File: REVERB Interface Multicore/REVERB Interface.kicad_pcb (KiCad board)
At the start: 2 copper layers, 90.2 x 95.9 mm, 71 parts, among them J1 RPiZeroW, J2 Iridium, J3 APRS, J4 Antenna, J5 UPDI, M1 MountingHole_Pad, M2 MountingHole_Pad, M3 MountingHole_Pad, M4 MountingHole_Pad, M5 PiMount, M6 PiMount, M7 PiMount, M8 PiMount, U1 IMU, U2 MAX3232, U3 ATtiny1604-SS, U4 TXB0104D, U5 DS3231BOB, U6 LM1117-3.3

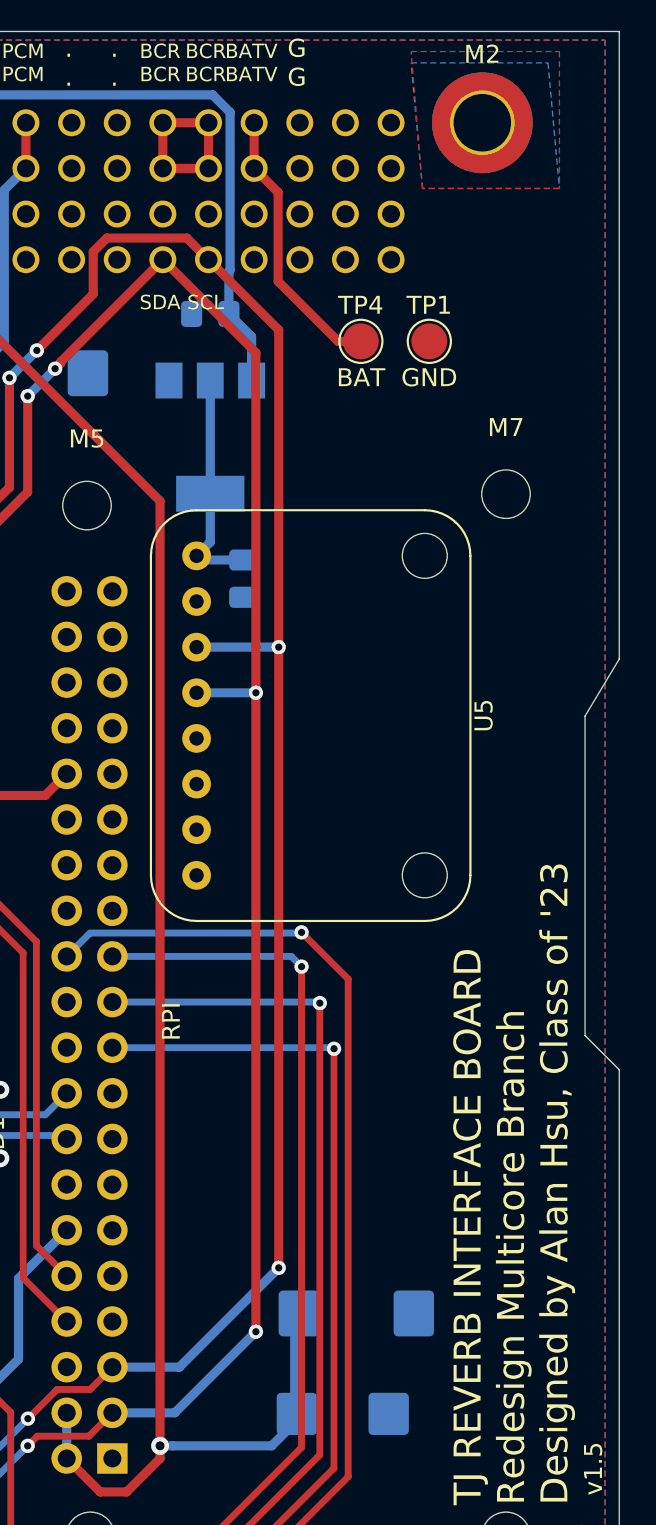
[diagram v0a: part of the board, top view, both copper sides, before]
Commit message: add footprints, may need to use smaller battery
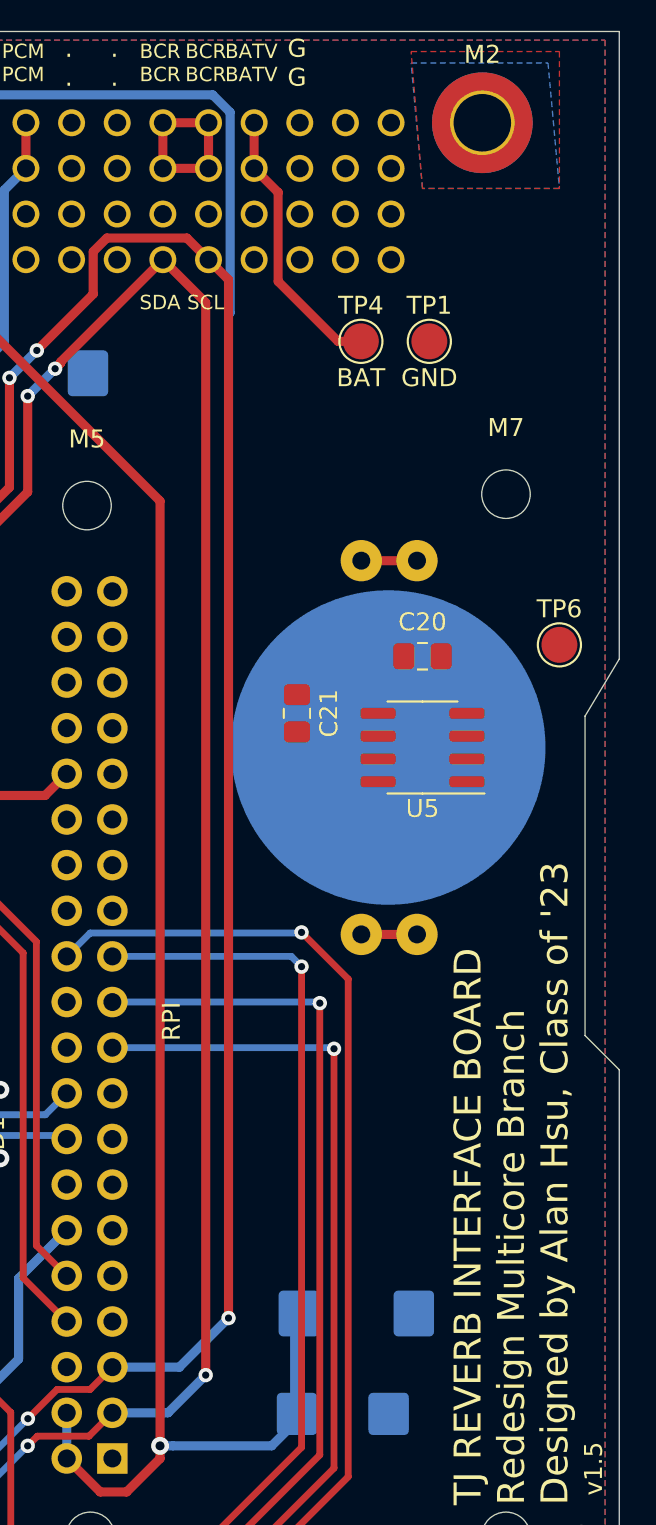
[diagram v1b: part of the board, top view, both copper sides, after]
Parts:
- removed U6: LM1117-3.3, Package_TO_SOT_SMD:SOT-223-3_TabPin2
- added BT1: CR-2032, REVERB Interface:CR2032-LINX-HLD-001-THM, B.Cu at (184.2, 92.7)
- added TP6: SQWV, TestPoint:TestPoint_Pad_D2.0mm, F.Cu at (193.7, 87.0)
- C20, C21: value 10uF -> 1uF; moved to F.Cu
- U5: value DS3231BOB -> DS3232M; footprint REVERB Interface:DS3231BOB -> Package_SO:SOIC-8_3.9x4.9mm_P1.27mm
- moved C20 22.4 mm to (186.1, 87.6)
- moved U5 12.7 mm to (186.1, 92.7), turned to 180 degrees
- moved C21 8.09 mm to (179.1, 90.8), turned to 90 degrees
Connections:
- C20 pad 1: /SW7 -> +3V3
- C21 pad 1: Net-(C21-Pad1) -> Net-(BT1-Pad1)
- H2 pad 16: /SW7 -> (no net)
- U5 pad 1: Net-(C21-Pad1) -> (no net)
- U5 pad 2: GND -> +3V3
- U5 pad 3: /EPSSCL -> /SQW
- U5 pad 4: /EPSSDA -> (no net)
- U5 pad 5: (no net) -> GND
- U5 pad 6: (no net) -> Net-(BT1-Pad1)
- U5 pad 7: (no net) -> /EPSSDA
- U5 pad 8: (no net) -> /EPSSCL
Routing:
- net /SW7: track 53.3 -> 0.00 mm
- net (no net): track 0.00 -> 49.1 mm
- net Net-(C21-Pad1): track 12.7 -> 0.00 mm
- net /EPSSCL: track 175.6 -> 168.7 mm, vias 9 -> 8
- net Net-(BT1-Pad1): track 0.00 -> 6.20 mm
- net /EPSSDA: track 181.2 -> 175.4 mm, vias 8 -> 7

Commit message: 3d model updates
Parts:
- moved C11 2.54 mm to (179.8, 124.2)
- moved C13 2.54 mm to (179.1, 129.8)
- moved C20 0.64 mm to (185.4, 87.6)
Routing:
- net +3V3: track 96.7 -> 156.8 mm
- net (no net): track 49.1 -> 0.00 mm
- net Net-(BT1-Pad1): track 6.20 -> 34.7 mm
- net /EPSSDA: track 175.4 -> 189.8 mm, vias 7 -> 9
- net /EPSSCL: track 168.7 -> 176.7 mm
- net /SQW: track 0.00 -> 7.78 mm
- net /SPISCK: track 72.9 -> 68.0 mm
- net /SPIMISO: track 73.1 -> 68.4 mm
- net /SPIMOSI: track 72.7 -> 68.6 mm
- net /SPICE0: track 87.1 -> 83.5 mm
- net +5V: track 183.5 -> 180.8 mm
- net GND: vias 25 -> 27

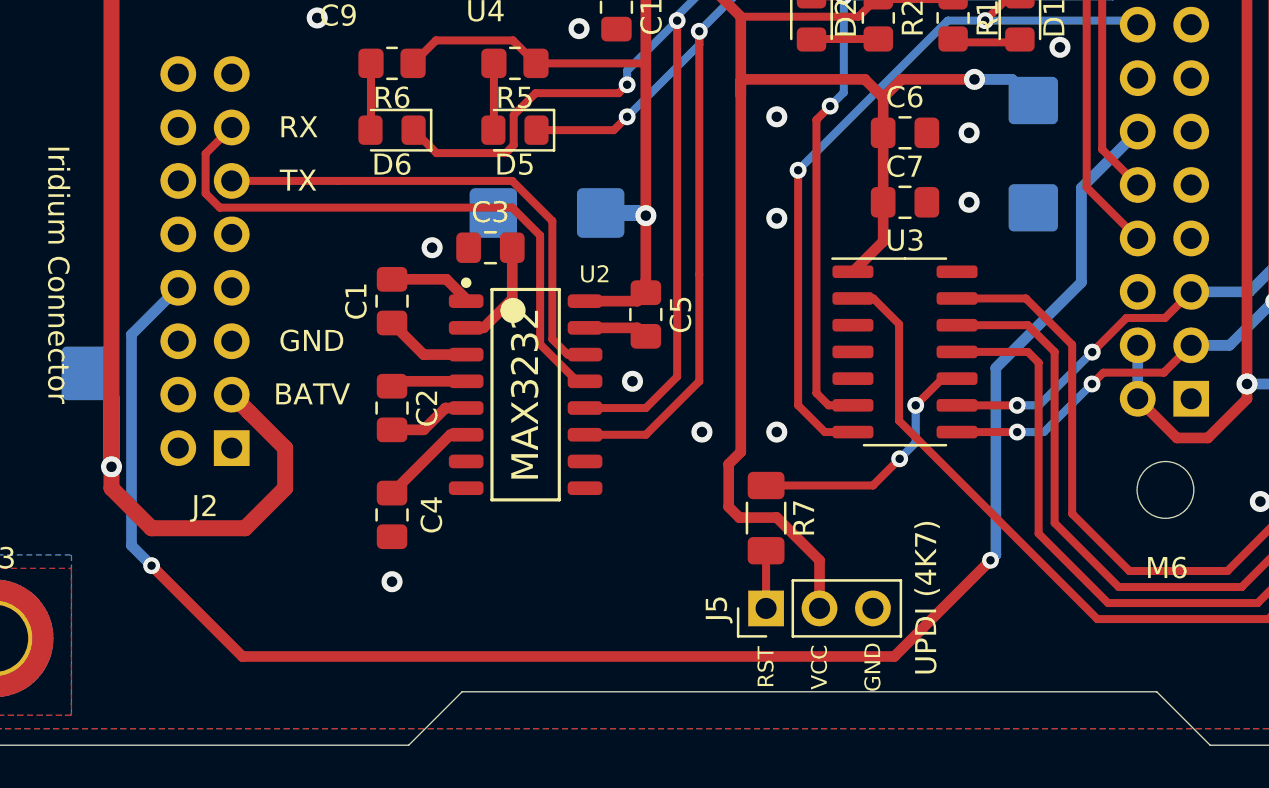
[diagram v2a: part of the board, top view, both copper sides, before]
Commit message: Remove RI line
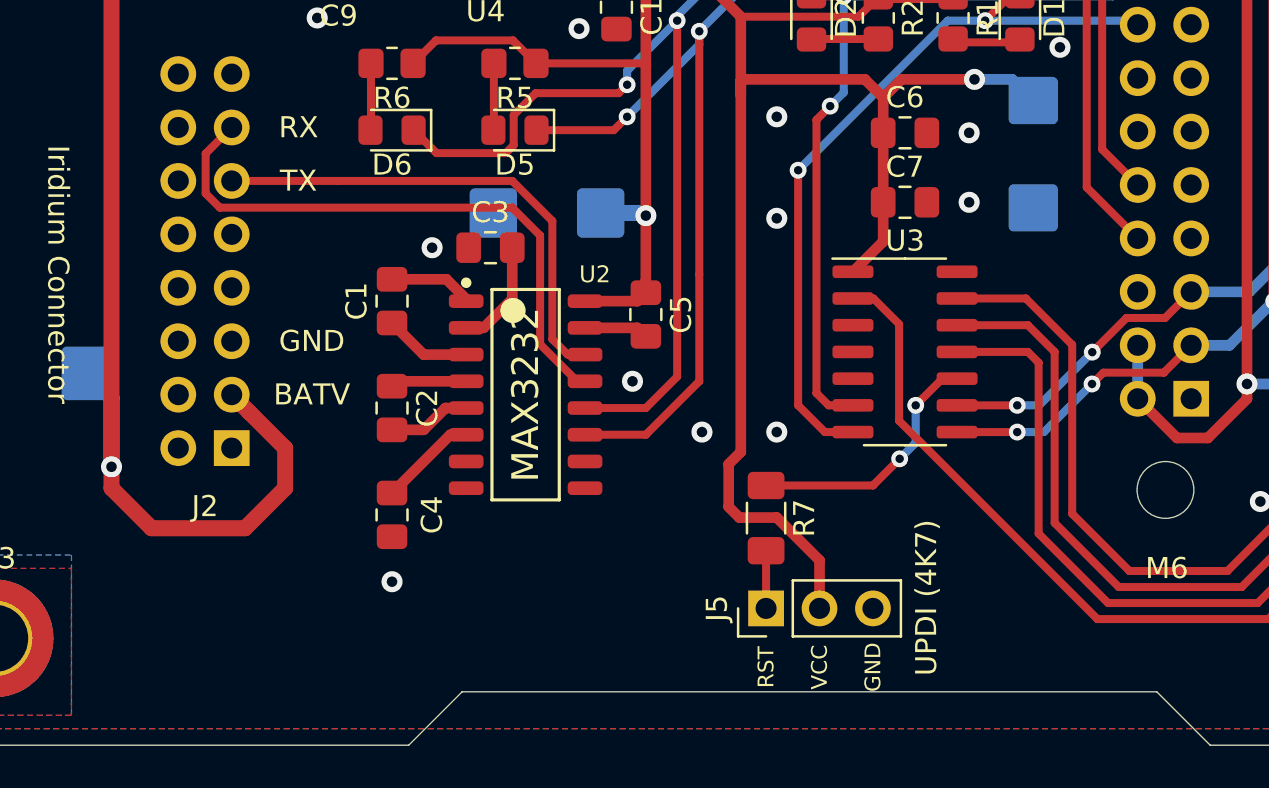
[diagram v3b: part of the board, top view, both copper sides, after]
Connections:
- J1 pad 12: /RI -> (no net)
- J2 pad 8: /RI -> (no net)
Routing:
- net /RI: track 81.4 -> 0.00 mm, vias 2 -> 0

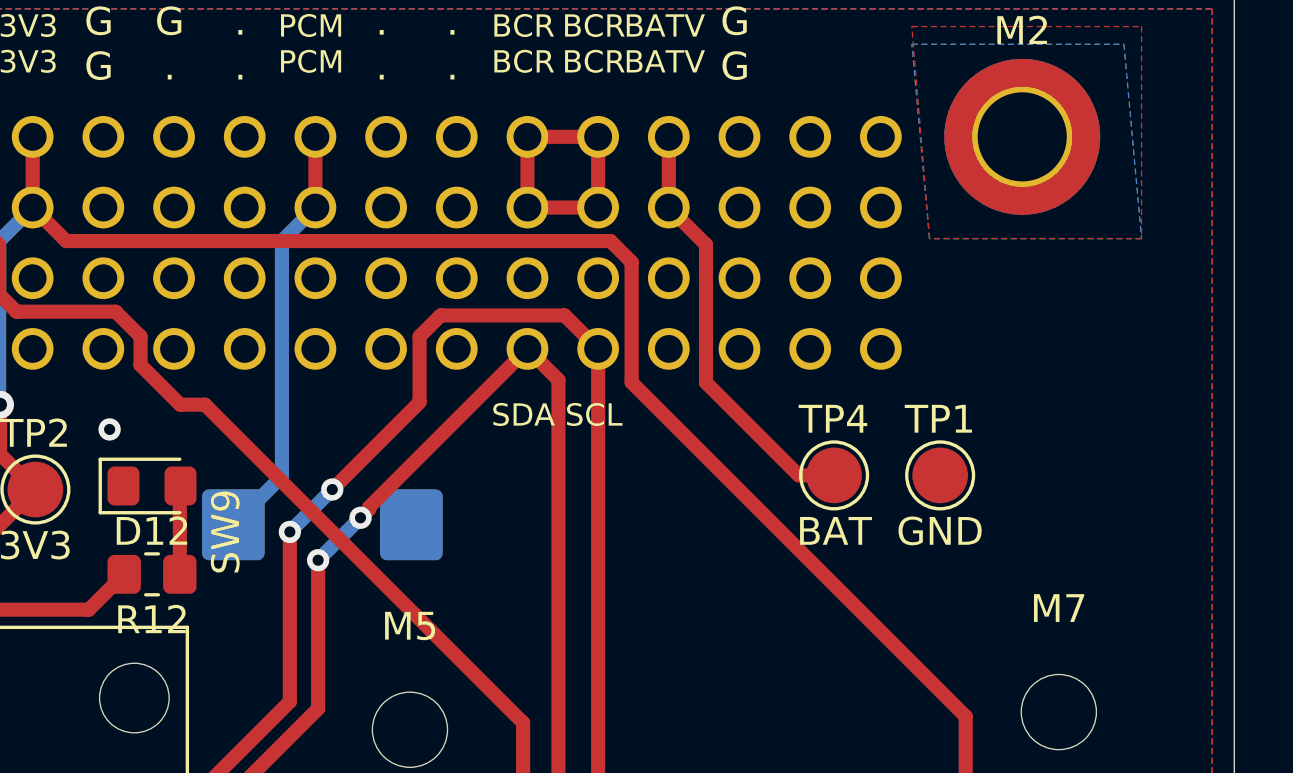
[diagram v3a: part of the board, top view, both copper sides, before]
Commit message: add usb switch
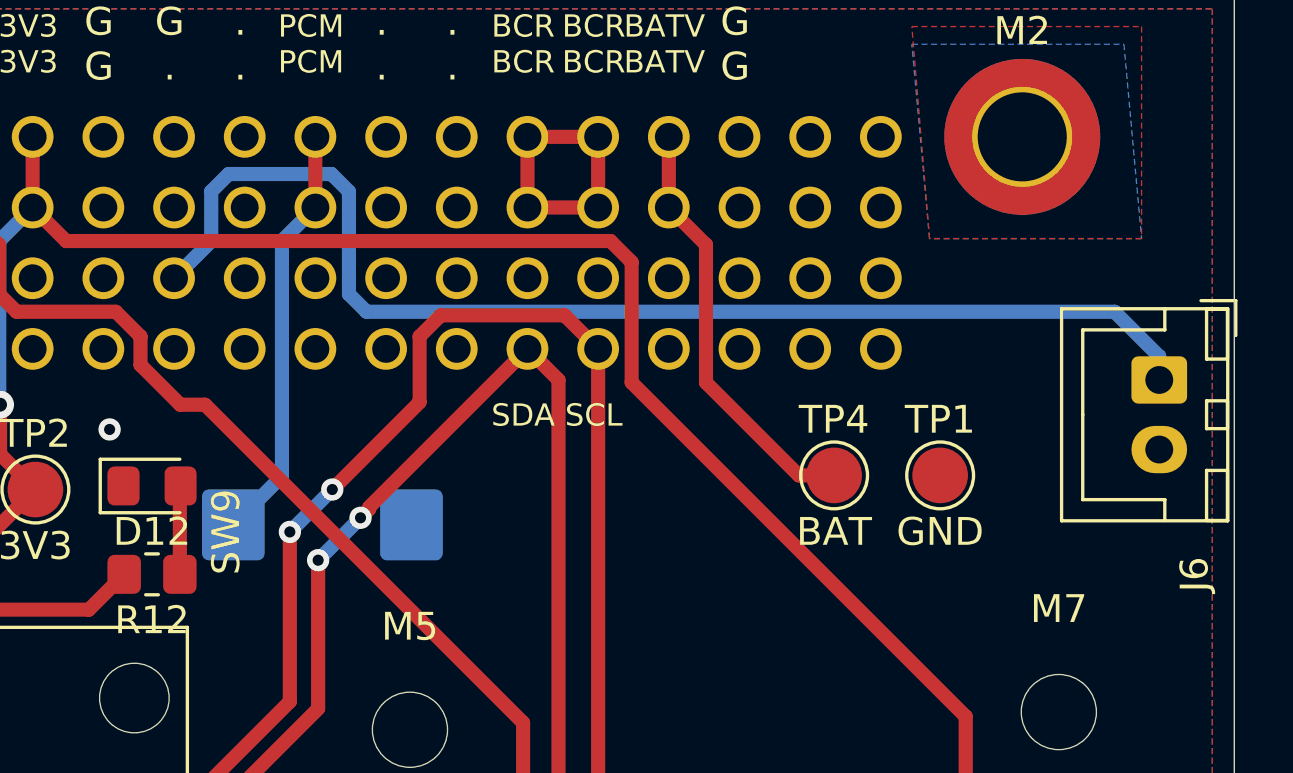
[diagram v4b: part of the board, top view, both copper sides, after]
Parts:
- added J6: USBPWR, Connector_JST:JST_XH_B2B-XH-A_1x02_P2.50mm_Vertical, F.Cu at (194.3, 66.7)
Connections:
- H1 pad 32: (no net) -> /5VUSBCHG
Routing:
- net /5VUSBCHG: track 0.00 -> 43.7 mm

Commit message: Move some parts around, remove UART LEDs, .step export, push v1.6
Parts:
- removed D1, D5: RED, LED_SMD:LED_0805_2012Metric_Pad1.15x1.40mm_HandSolder
- removed D2, D6: GREEN, LED_SMD:LED_0805_2012Metric_Pad1.15x1.40mm_HandSolder
- removed R1, R2, R5, R6: 1K, Resistor_SMD:R_0805_2012Metric_Pad1.20x1.40mm_HandSolder
- moved R11 9.58 mm to (109.2, 70.9), turned to 180 degrees
- moved D11 8.18 mm to (109.2, 74.5), turned to 180 degrees
- moved C9 7.73 mm to (132.1, 119.1), turned to 0 degrees
- moved C10 3.98 mm to (139.7, 117.2)
- moved U4 3.98 mm to (133.5, 112.1)
- moved JP1 3.86 mm to (145.4, 101.6)
- moved JP2 3.86 mm to (154.3, 101.7)
- moved JP3 3.86 mm to (145.4, 108.0)
- moved JP4 3.86 mm to (154.3, 108.0)
- moved C16 3.81 mm to (112.0, 82.3), turned to 270 degrees
- moved C15 3.21 mm to (113.0, 103.5), turned to 90 degrees
- moved J3 3.18 mm to (117.5, 85.1)
- moved J2 3.17 mm to (120.0, 134.6)
- moved BT1 2.29 mm to (181.9, 92.7)
- moved C11 2.29 mm to (177.5, 124.2)
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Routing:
- net /R1OUT: track 52.4 -> 34.6 mm, vias 3 -> 2
- net /T1IN: track 54.2 -> 41.3 mm, vias 3 -> 2
- net /SW10: track 139.2 -> 129.3 mm
- net /SW8: track 100.5 -> 90.8 mm
- net /APRSTXSh: track 24.2 -> 31.0 mm
- net /APRSRXSh: track 28.0 -> 34.6 mm
- net +5V: track 180.8 -> 187.2 mm
- net /SW6: track 54.0 -> 48.0 mm
- net +3V3: track 156.8 -> 160.8 mm
- net Net-(D1-Pad2): track 3.30 -> 0.00 mm
- net /R1IN: track 28.3 -> 31.5 mm
- net Net-(D6-Pad2): track 3.19 -> 0.00 mm
- net Net-(D2-Pad2): track 3.19 -> 0.00 mm
- net Net-(D5-Pad2): track 3.19 -> 0.00 mm
- net /T1OUT: track 23.4 -> 26.6 mm
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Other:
- board text added: "G"
- board text added: "v1.6"
- board text removed: "v1.5"

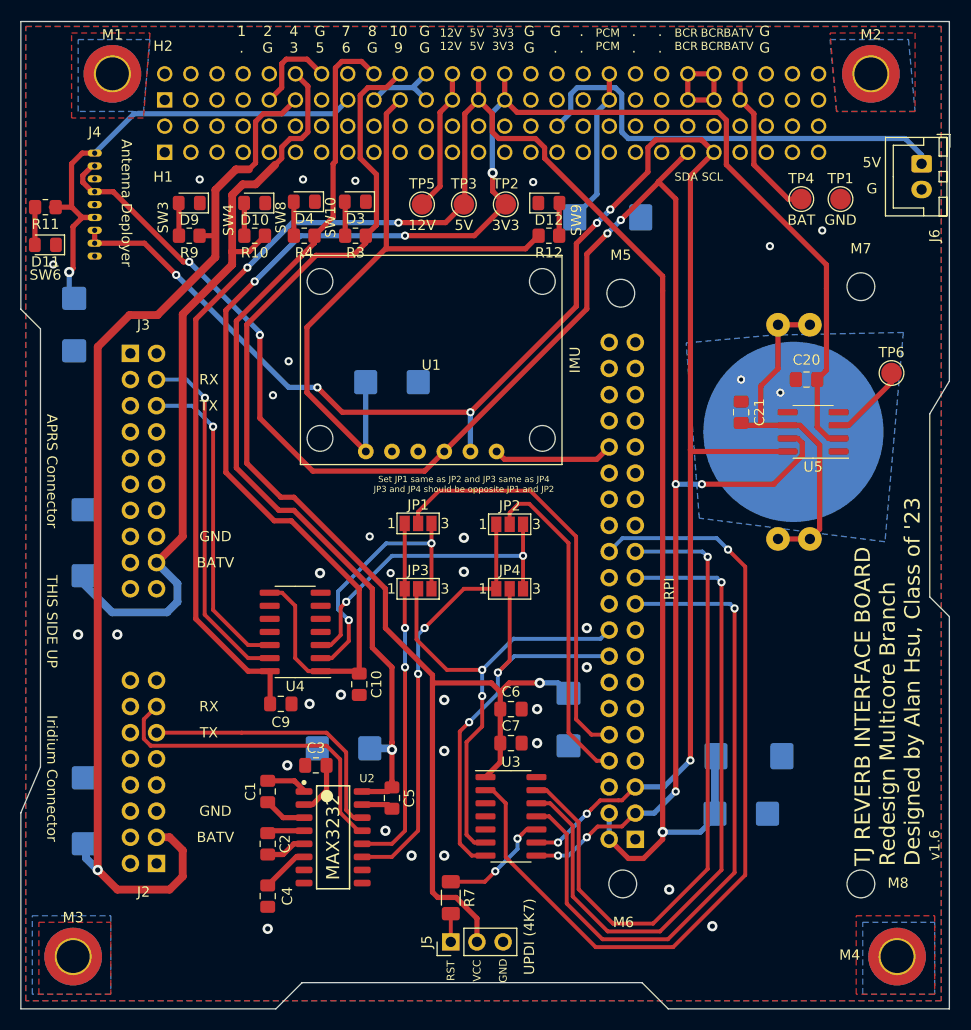
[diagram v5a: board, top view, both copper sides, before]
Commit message: add i2c0 option
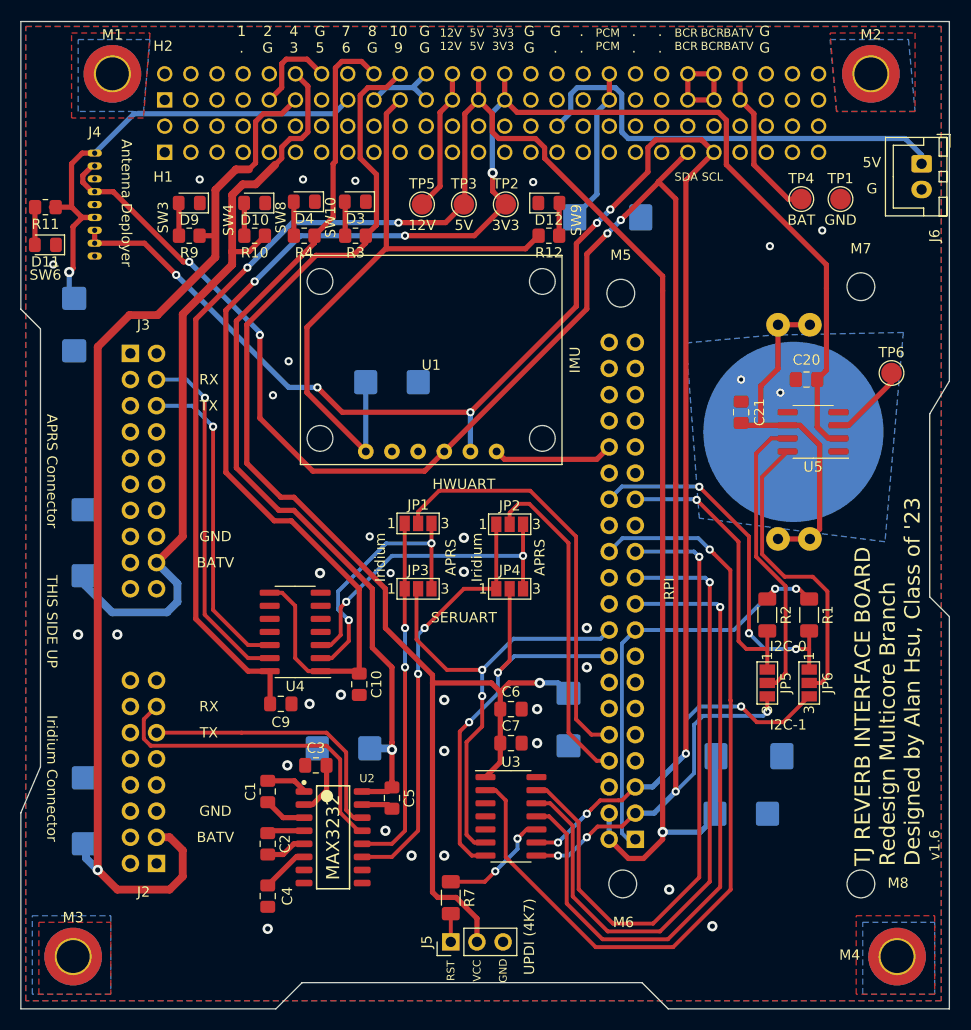
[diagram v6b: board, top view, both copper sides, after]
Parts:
- added JP5: RTCSDA, Jumper:SolderJumper-3_P1.3mm_Open_Pad1.0x1.5mm_NumberLabels, F.Cu at (179.3, 117.1)
- added JP6: RTCSCL, Jumper:SolderJumper-3_P1.3mm_Open_Pad1.0x1.5mm_NumberLabels, F.Cu at (183.4, 117.1)
- added R1: 2.2K, Resistor_SMD:R_1206_3216Metric_Pad1.30x1.75mm_HandSolder, F.Cu at (183.4, 110.5)
- added R2: 2.2K, Resistor_SMD:R_1206_3216Metric_Pad1.30x1.75mm_HandSolder, F.Cu at (179.3, 110.5)
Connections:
- J1 pad 1: (no net) -> +3.3VA
- J1 pad 17: (no net) -> +3.3VA
- J1 pad 27: (no net) -> /SDA0
- J1 pad 28: (no net) -> /SCL0
- U5 pad 7: /EPSSDA -> /RTCSDA
- U5 pad 8: /EPSSCL -> /RTCSCL
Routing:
- net +3.3VA: track 0.00 -> 42.1 mm, vias 0 -> 2
- net /SCL0: track 0.00 -> 35.7 mm, vias 0 -> 3
- net /RTCSCL: track 0.00 -> 29.1 mm
- net /RTCSDA: track 0.00 -> 28.3 mm
- net /SDA0: track 0.00 -> 28.2 mm, vias 0 -> 1
- net /EPSSCL: track 176.2 -> 183.5 mm, vias 8 -> 9
- net /SPICE0: track 82.3 -> 80.3 mm
- net /SPIMOSI: track 66.3 -> 64.4 mm
- net /SPIMISO: track 66.1 -> 64.5 mm
- net /SPISCK: track 65.6 -> 64.4 mm
- net /EPSSDA: vias 9 -> 8
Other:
- board text added: "APRS"
- board text added: "HWUART"
- board text added: "I2C-0"
- board text added: "I2C-1"
- board text added: "Iridium"
- board text added: "SERUART"
- board text removed: "Set JP1 same as JP2 and JP3 same as JP4 JP3 and JP4 should be opposite JP1 and JP2"

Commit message: finish tidying up schematics
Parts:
- M1, M2, M3, M4: value MountingHole_Pad -> Stack Mounting Hole
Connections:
- net Net-(BT1-Pad1) renamed +BATT

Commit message: new gerber exports
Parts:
- C13, C16: value 47uF -> 22uF
